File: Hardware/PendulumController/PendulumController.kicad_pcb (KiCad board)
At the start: 2 copper layers, 157 x 47 mm, 60 parts, among them J101 MOTOR, J102 ENCODER, J201 ICSP, J302 19V Input, J401 USB_B_Micro, J402 PROG, SW201 RESET, SW202 START_SW, SW203 STOP/MODE_SW, U201 ATmega328P, U301 NCV1117ST50T3G, U401 FT232RL, Y201 16mHz

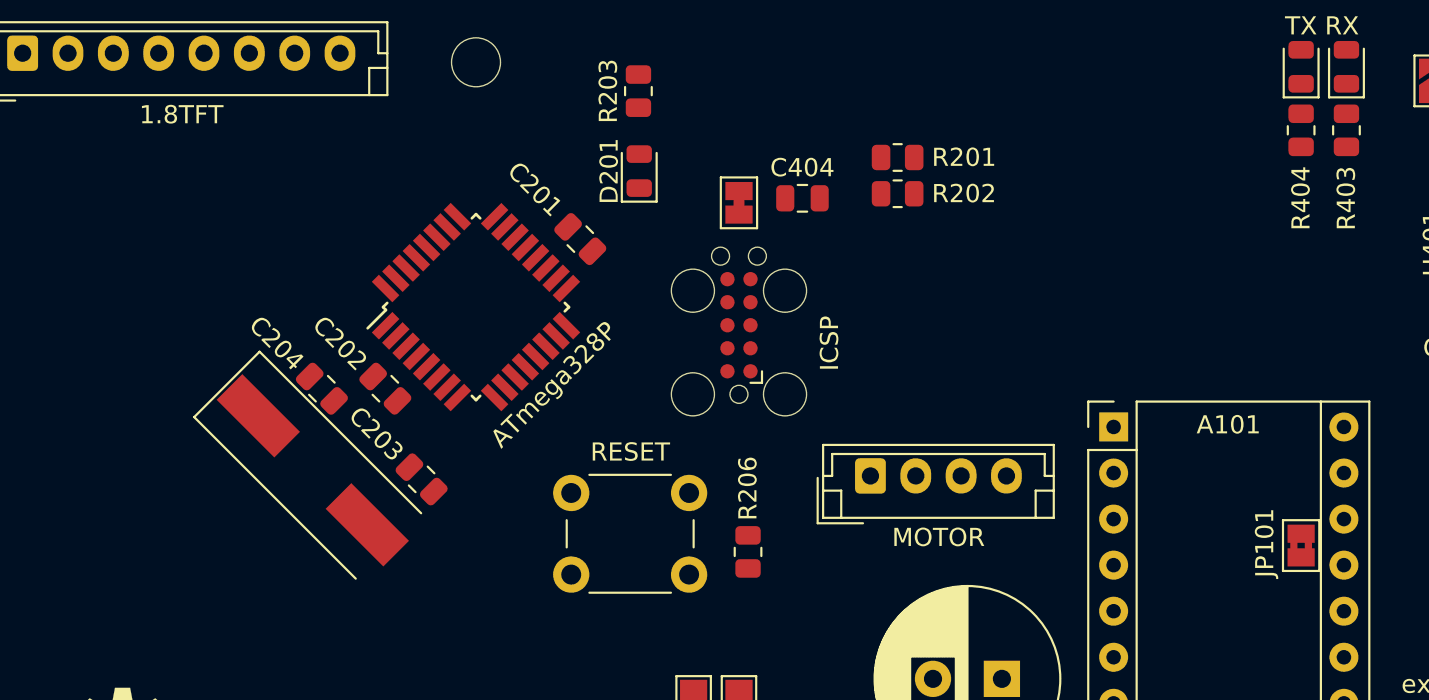
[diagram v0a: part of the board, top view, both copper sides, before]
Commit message: Check backlight power circuit before printing
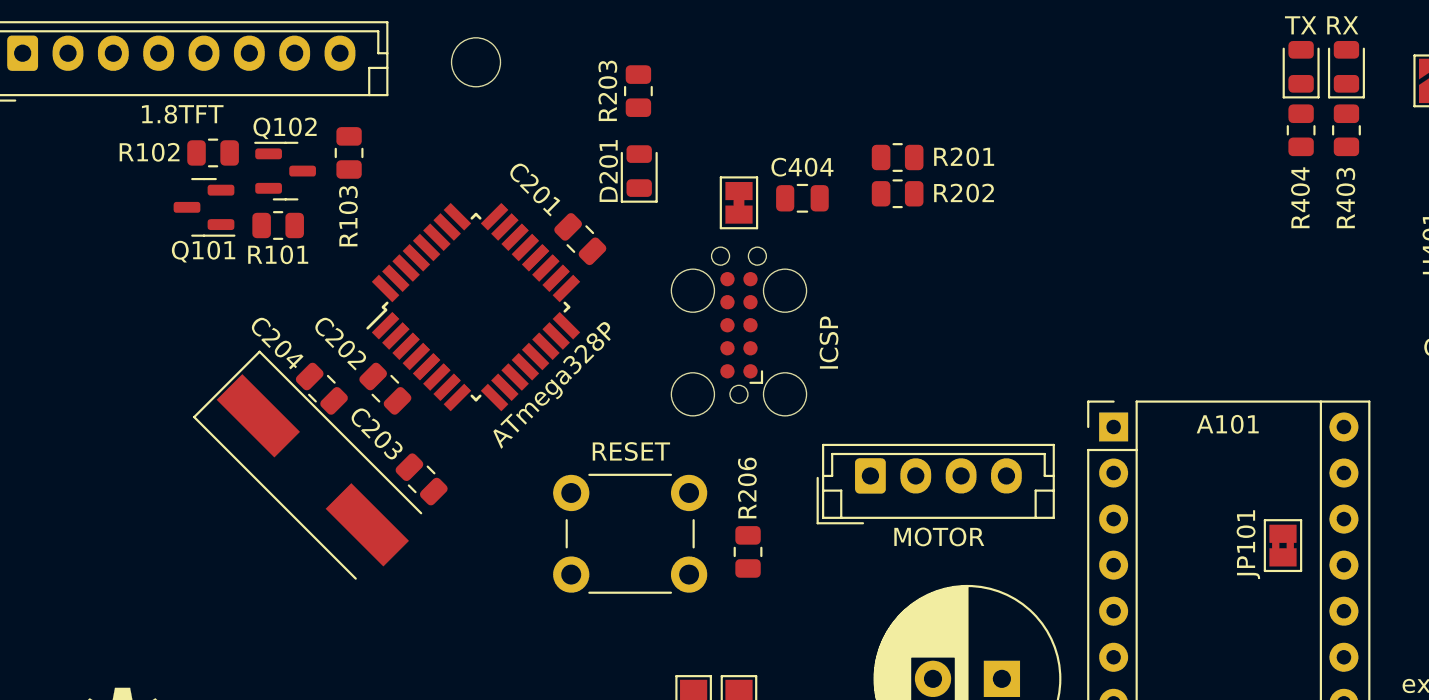
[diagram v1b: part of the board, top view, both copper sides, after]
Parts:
- added Q101: MMBT3904, Package_TO_SOT_SMD:SOT-23, F.Cu at (130.0, 78.0)
- added Q102: MMBT3906, Package_TO_SOT_SMD:SOT-23, F.Cu at (134.5, 76.0)
- added R101: 10K, Resistor_SMD:R_0805_2012Metric, F.Cu at (134.1, 79.0)
- added R102: 2K2, Resistor_SMD:R_0805_2012Metric, F.Cu at (130.5, 75.0)
- added R103: TBD, Resistor_SMD:R_0805_2012Metric, F.Cu at (138.0, 75.0)
- moved JP101 1.00 mm to (189.5, 96.7)
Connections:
- A101 pad 14: Net-(A101-Pad14) -> /EN
- D101 pad 8: unconnected-(D101-Pad8) -> /TFT_LED
- JP101 pad 2: Net-(A101-Pad14) -> /EN
- U201 pad 11: /MCU/STOP/MODE -> unconnected-(U201-Pad11)
- U201 pad 12: /STEP -> /MCU/STOP/MODE
- U201 pad 13: /DIR -> /MCU/START
- U201 pad 14: /MCU/START -> unconnected-(U201-Pad14)
- U201 pad 23: /MCU/AnalogP -> /STEP
- U201 pad 24: /MCU/AnalogI -> /DIR
- U201 pad 25: /MCU/AnalogD -> /EN
- U201 pad 26: unconnected-(U201-Pad26) -> /MCU/AnalogP
- U201 pad 27: /SDA -> /MCU/AnalogI
- U201 pad 28: /SCL -> /MCU/AnalogD

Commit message: USB C!
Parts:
- added R405: 5K1, Resistor_SMD:R_0805_2012Metric, F.Cu at (220.0, 86.0)
- added R406: 5K1, Resistor_SMD:R_0805_2012Metric, F.Cu at (217.9, 86.0)
- C101: value 10uf -> 470uF
- J401: value USB_B_Micro -> USBC; footprint Connector_USB:USB_Mini-B_Lumberg_2486_01_Horizontal -> Connector_USB:USB_C_Receptacle_XKB_U262-16XN-4BVC11
- R102: value 2K2 -> TBD
- moved R401 5.46 mm to (213.0, 87.5), turned to 0 degrees
- moved R402 3.35 mm to (209.5, 87.5), turned to 0 degrees
- moved C401 2.50 mm to (212.0, 74.0)
- moved C402 2.50 mm to (208.5, 74.0)
- moved C403 2.50 mm to (205.2, 85.8)
- moved U401 2.50 mm to (206.5, 80.0)
- moved J401 1.87 mm to (219.5, 78.5)
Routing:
- net /MCU/SDO: track 0.00 -> 14.8 mm, vias 0 -> 2
- net Net-(C204-Pad1): track 0.00 -> 12.6 mm
- net /Programming/USB-: track 0.00 -> 10.6 mm
- net /MCU/SDI: track 0.00 -> 9.40 mm
- net Net-(C203-Pad1): track 0.00 -> 9.17 mm
- net /Programming/USB+: track 0.00 -> 8.53 mm
- net +5V: track 0.00 -> 8.24 mm
- added copper zone on F.Cu, net +5V
